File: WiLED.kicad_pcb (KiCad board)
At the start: 2 copper layers, 37 x 83 mm, 54 parts, among them P1 Serial to USB, P2 DC In, P3 Lamp Connector, P4 LED Out, SW1 Reset, SW2 Boot, SW3 Toggle, SW4 Rotary Encoder, U1 ESP-WROOM-32, U2 VXO7803-500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

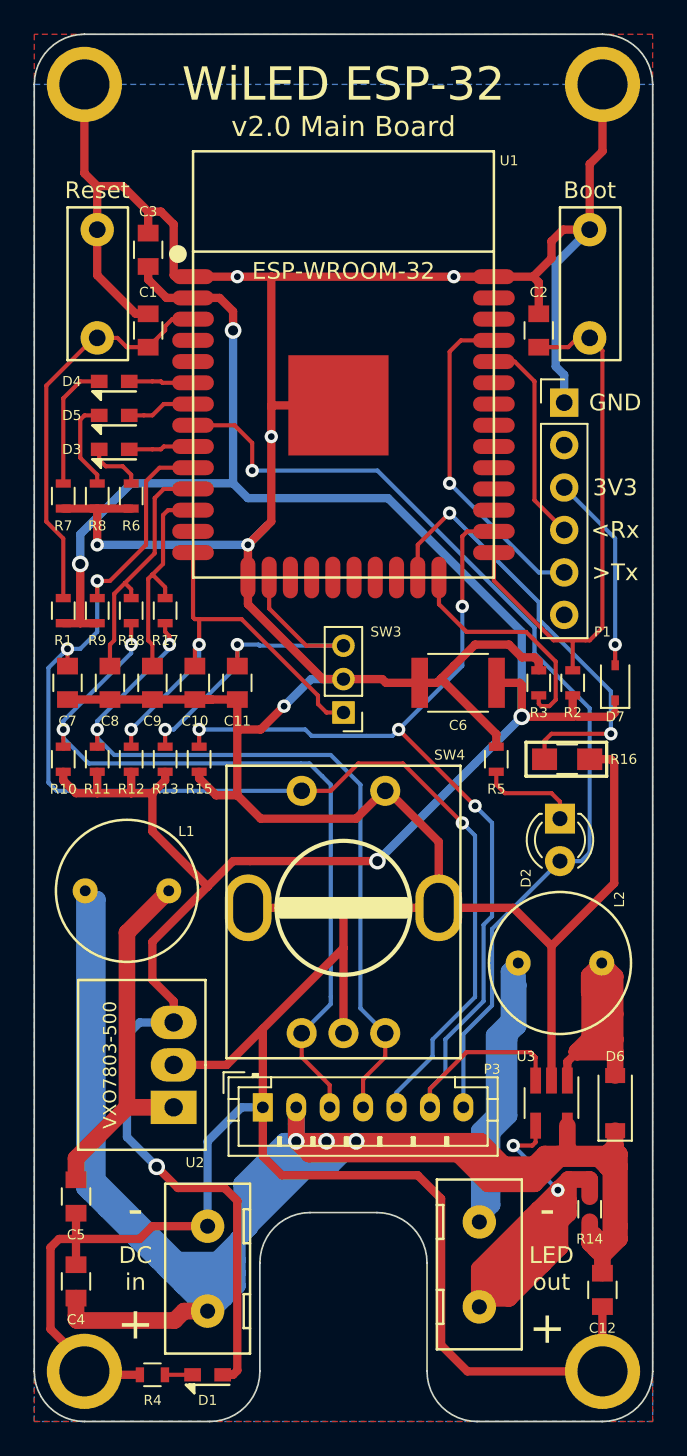
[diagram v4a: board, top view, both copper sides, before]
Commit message: Add stitching vias to PCB
The PCB now has numerous stitching vias for the ground planes.
Also made some of the silk screen text slightly larger.
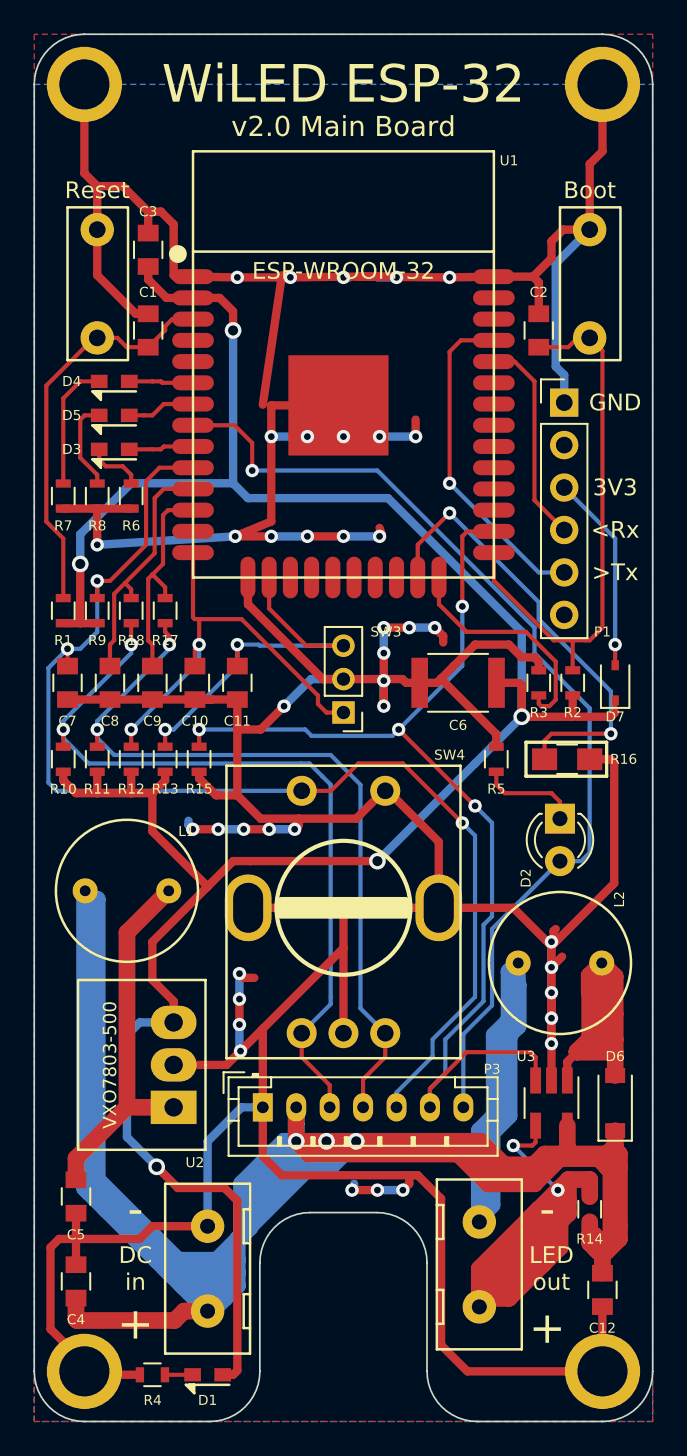
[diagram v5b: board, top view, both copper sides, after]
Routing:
- net GND: track 327.7 -> 391.3 mm, vias 6 -> 40

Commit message: Add PIR sensor and more stitching vias
Added a connection for a HC-SR501 PIR sensor, to a spare GPIO on the
ESP-32.
Also increased the number of stitching vias.
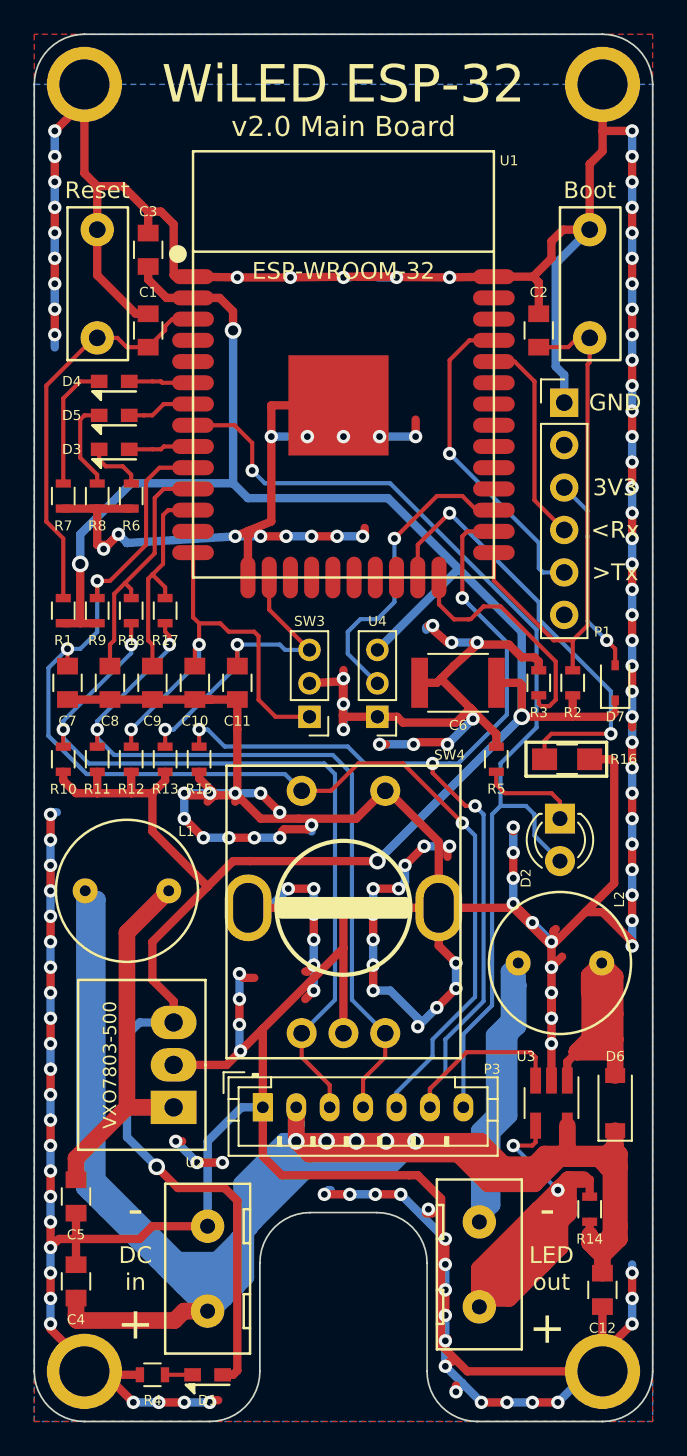
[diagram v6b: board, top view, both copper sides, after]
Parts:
- added U4: HC-SR501, Pin_Headers:Pin_Header_Straight_1x03_Pitch2.00mm, F.Cu at (174.8, 92.2)
- moved SW3 2.05 mm to (170.7, 92.2)
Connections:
- U1 pad 27: Net-(U1-Pad27) -> PIR_TRG
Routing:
- net GND: track 391.3 -> 587.8 mm, vias 40 -> 161
- net RAW: track 199.6 -> 220.8 mm, vias 3 -> 5
- net PIR_TRG: track 0.00 -> 18.5 mm, vias 0 -> 1
- net +3V3: track 150.8 -> 157.7 mm
- net LED_PWM: track 65.2 -> 69.1 mm
- net TGL_2: track 23.1 -> 19.3 mm
- net IND_PWM: track 60.4 -> 62.7 mm
- net ENC_SW: track 73.0 -> 71.3 mm
- net IO0: track 32.7 -> 31.5 mm
- net LED_POS: track 48.8 -> 49.7 mm
- net CON_A: track 47.6 -> 48.3 mm
- net IO2: track 14.0 -> 14.7 mm

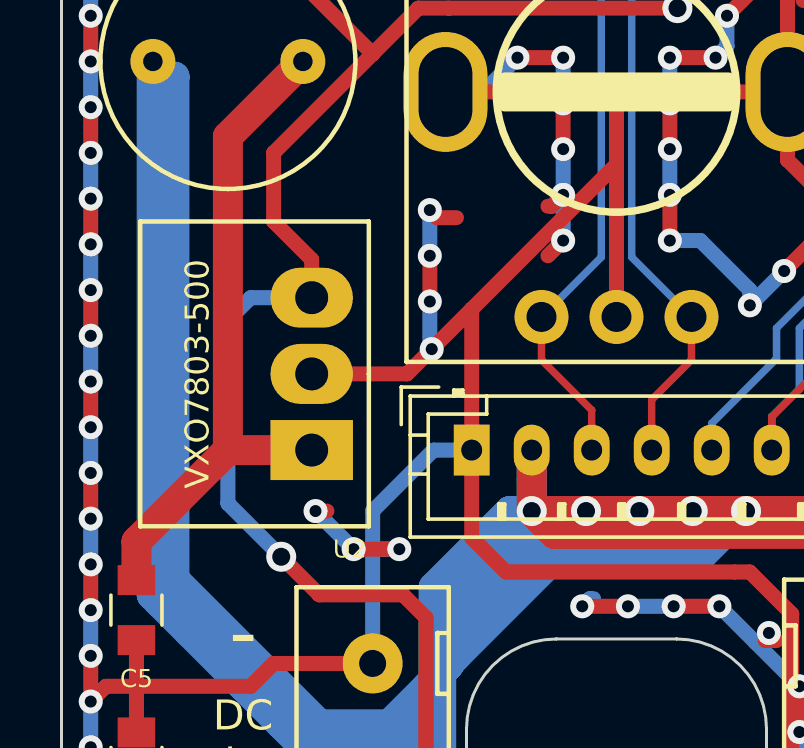
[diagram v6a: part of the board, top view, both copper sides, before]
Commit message: Add OSHW logo to silkscreen
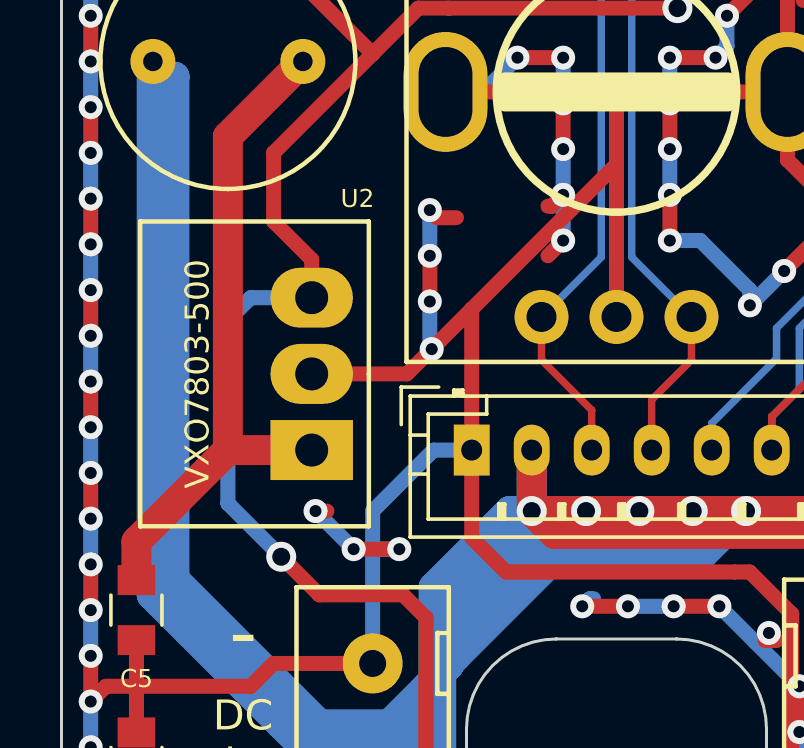
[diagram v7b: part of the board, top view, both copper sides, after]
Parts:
- added REF***: OSHW-Logo_19x20mm_SilkScreen, Symbols:OSHW-Logo_19x20mm_SilkScreen, B.Cu at (172.7, 77.1)
- added REF***: WEEE-Logo_5.6x8mm_SilkScreen, Symbols:WEEE-Logo_5.6x8mm_SilkScreen, B.Cu at (186.4, 115.6)

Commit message: Add input voltage to silkscreen
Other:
- board text added: "24-36 V"
- board text added: "DC"
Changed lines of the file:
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@@
 (kicad_pcb (version 4) (host pcbnew 4.0.6+dfsg1-1)
   (general
-    (links 0)
+    (links 112)
     (no_connects 0)
     (area 154.169999 51.315999 191.270001 134.416001)
     (thickness 1.6)
-    (drawings 44)
+    (drawings 46)
     (tracks 1124)
     (zones 0)
@@
   (title_block
     (title "WiLED ESP32 Base")
-    (date 2018-07-08)
+    (date 2018-07-09)
     (rev 2.0)
     (comment 4 "Released under the CERN Open Hardware Licence v1.2")
@@
     (mod_text_size 1 1)
     (mod_text_width 0.15)
-    (pad_size 2.8 4)
-    (pad_drill 1.8)
+    (pad_size 1.5 1.3)
+    (pad_drill 0)
     (pad_to_mask_clearance 0)
     (aux_axis_origin 172.72 134.366)
@@
     (visible_elements FFFFFF7F)
     (pcbplotparams
-      (layerselection 0x010f8_80000001)
+      (layerselection 0x010f0_80000001)
       (usegerberextensions true)
       (excludeedgelayer true)
@@
       (plotinvisibletext false)
       (padsonsilk false)
-      (subtractmaskfromsilk false)
+      (subtractmaskfromsilk true)
       (outputformat 1)
       (mirror false)
@@
     (descr "LED, diameter 3.0mm, 2 pins")
     (tags "LED diameter 3.0mm 2 pins")
-    (fp_text reference D2 (at 3.556 2.032 450) (layer F.SilkS)
+    (fp_text reference D2 (at 1.268 -2.846 540) (layer F.SilkS)
       (effects (font (size 0.6 0.6) (thickness 0.12)))
     )
@@
   (module custom-footprints:THT_Inductor_5mm (layer F.Cu)
     (at 185.674 106.934 180)
-    (fp_text reference L2 (at -3.556 3.81 270) (layer F.SilkS)
+    (fp_text reference L2 (at -3.556 3.81 360) (layer F.SilkS)
       (effects (font (size 0.6 0.6) (thickness 0.12)))
     )
@@
     (fp_line (start 2.35 0.9) (end 2.35 -0.9) (layer F.CrtYd) (width 0.05))
     (fp_line (start 2.35 0.9) (end -2.35 0.9) (layer F.CrtYd) (width 0.05))
-    (pad 1 smd rect (at -1.35 0) (size 1.5 1.3) (layers F.Cu F.Paste F.Mask)
+    (pad 1 smd rect (at -1.35 0) (size 1.5 1.3) (layers F.Cu F.Mask)
       (net 48 "Net-(R16-Pad1)"))
     (pad 2 smd rect (at 1.35 0) (size 1.5 1.3) (layers F.Cu F.Mask)
@@
       (xy 2.823256 3.900663)) (layer B.SilkS) (width 0.01))
   )
+  (gr_text DC (at 176.12 120.766) (layer F.SilkS)
+    (effects (font (size 0.7 0.7) (thickness 0.15)))
+  )
+  (gr_text "24-36 V" (at 171.92 120.366) (layer F.SilkS)
+    (effects (font (size 1 1) (thickness 0.22)))
+  )
   (gr_line (start 190.246 94.615) (end 190.246 94.869) (layer B.SilkS) (width 0.2))
